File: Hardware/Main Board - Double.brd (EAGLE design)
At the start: 124.5 x 73.7 mm, 112 parts, among them J1 MICROMOD-2222-C, J10 MICRO-SD-PUSH-PUSH-EXT-PIN, J2 Vertical Qwiic Connector, J4 QWIIC_RIGHT_ANGLE, J5 CORTEX_JTAG_DEBUG_MINIMUM_PTH, J6 MICROMOD_FUNCTION_MAIN, J7 MICROMOD_FUNCTION_MAIN, Q1 3.1A/30V/105mΩ, U1 STG3856QTR, U2 MCP73831, U5 AP7361C-33

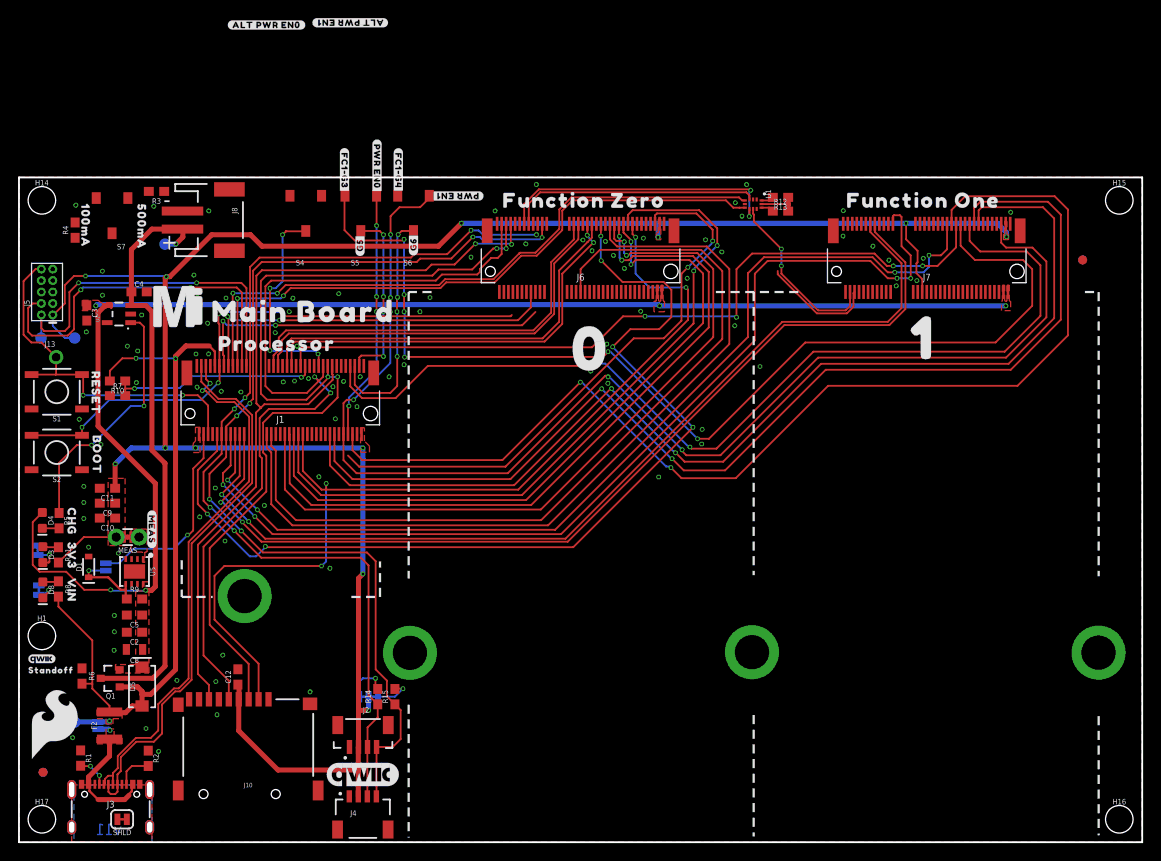
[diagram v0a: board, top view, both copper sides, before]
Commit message: Routes airwires
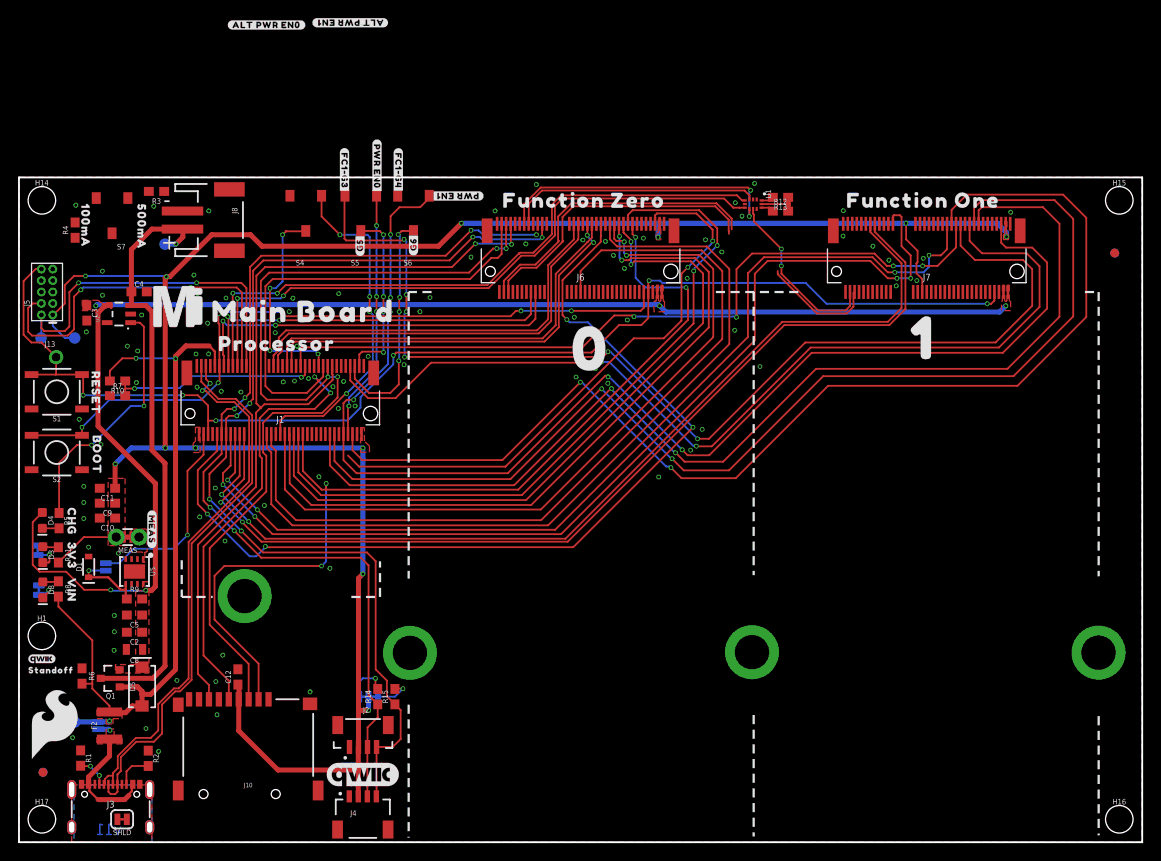
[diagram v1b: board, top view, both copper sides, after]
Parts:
- moved FD1 3.64 mm to (121.4, 65.3)
- moved FD2 3.64 mm to (121.4, 65.3)
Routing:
- net !RESET!: track 40.9 -> 140.2 mm, vias 2 -> 6
- net A1-PROCESSOR/!CS0!-ALT: track 0.00 -> 37.3 mm, vias 0 -> 4
- net RX1-AUX_TX-FC0-PLEX: track 0.00 -> 33.8 mm
- net TX1-AUX_RX-FC0-PLEX: track 0.00 -> 33.0 mm
- net !BOOT!: track 64.2 -> 80.9 mm, vias 4 -> 6
- net D0-PROCESSOR: track 108.7 -> 103.5 mm, vias 6 -> 4
- net RTS1-PROCESSOR: track 40.4 -> 43.1 mm
- net !CS1!-PROCESSOR: track 125.7 -> 128.2 mm
- net SPI_SDO1-PROCESSOR: track 123.0 -> 125.4 mm
- net G7-PROCESSOR: track 107.3 -> 106.0 mm
- net TX1-PROCESSOR: track 70.7 -> 71.5 mm
- net RX1-PROCESSOR: track 69.9 -> 70.7 mm
- net SPI_SCK1-PROCESSOR: track 120.6 -> 121.4 mm
- net G5-PROCESSOR: track 119.4 -> 120.2 mm
- net VCC: track 156.5 -> 157.0 mm
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
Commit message: Large rework in which many of the traces were routed to leave more space between them.
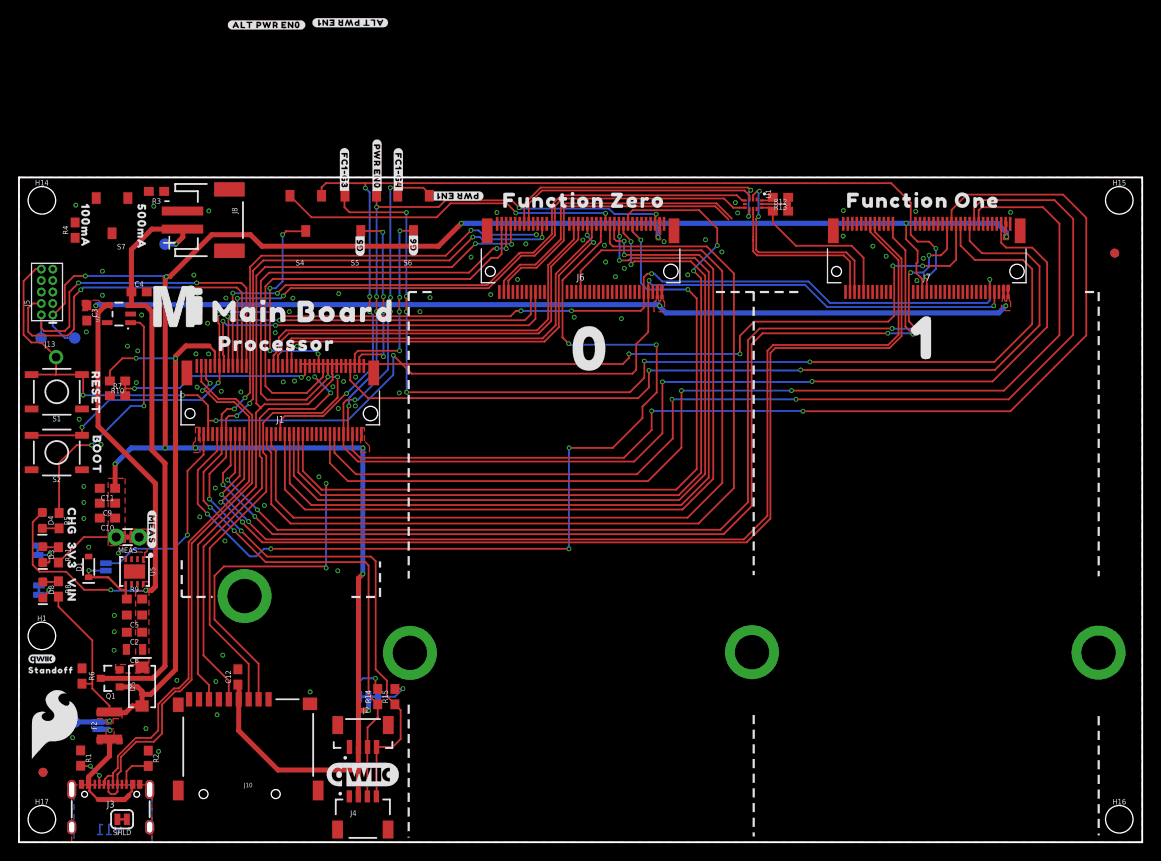
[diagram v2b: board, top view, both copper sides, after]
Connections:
- removed net PWR_EN0: J6.71
- net SDIO_DATA2/PWR_EN0_ALT: now also J6.71
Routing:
- net A1-PROCESSOR/!CS0!-ALT: track 37.3 -> 114.6 mm, vias 4 -> 6
- net PWR_EN0: track 63.8 -> 0.00 mm, vias 2 -> 0
- net !BOOT!: track 80.9 -> 126.2 mm, vias 6 -> 8
- net !CS0!-PROCESSOR: track 0.00 -> 38.3 mm, vias 0 -> 2
- net SDIO_DATA2/PWR_EN0_ALT: track 27.7 -> 60.8 mm, vias 4 -> 6
- net !DFU-FC1!: track 1.41 -> 18.1 mm
- net RX2-PROCESSOR: track 106.3 -> 118.3 mm
- net TX2-PROCESSOR: track 107.9 -> 119.8 mm
- net G4-PROCESSOR/SD_CARD_!CS!: track 109.3 -> 120.9 mm
- net G3-PROCESSOR: track 80.5 -> 91.4 mm
- net TX1-AUX_RX-FC1-PLEX: track 12.5 -> 22.9 mm, vias 0 -> 2
- net PWM0-PROCESSOR: track 92.7 -> 102.8 mm
- net G2-PROCESSOR: track 78.2 -> 88.4 mm
- net G1-PROCESSOR: track 81.8 -> 91.8 mm
- net D1-PROCESSOR: track 109.4 -> 119.1 mm, vias 4 -> 6
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
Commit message: Routes more airwires
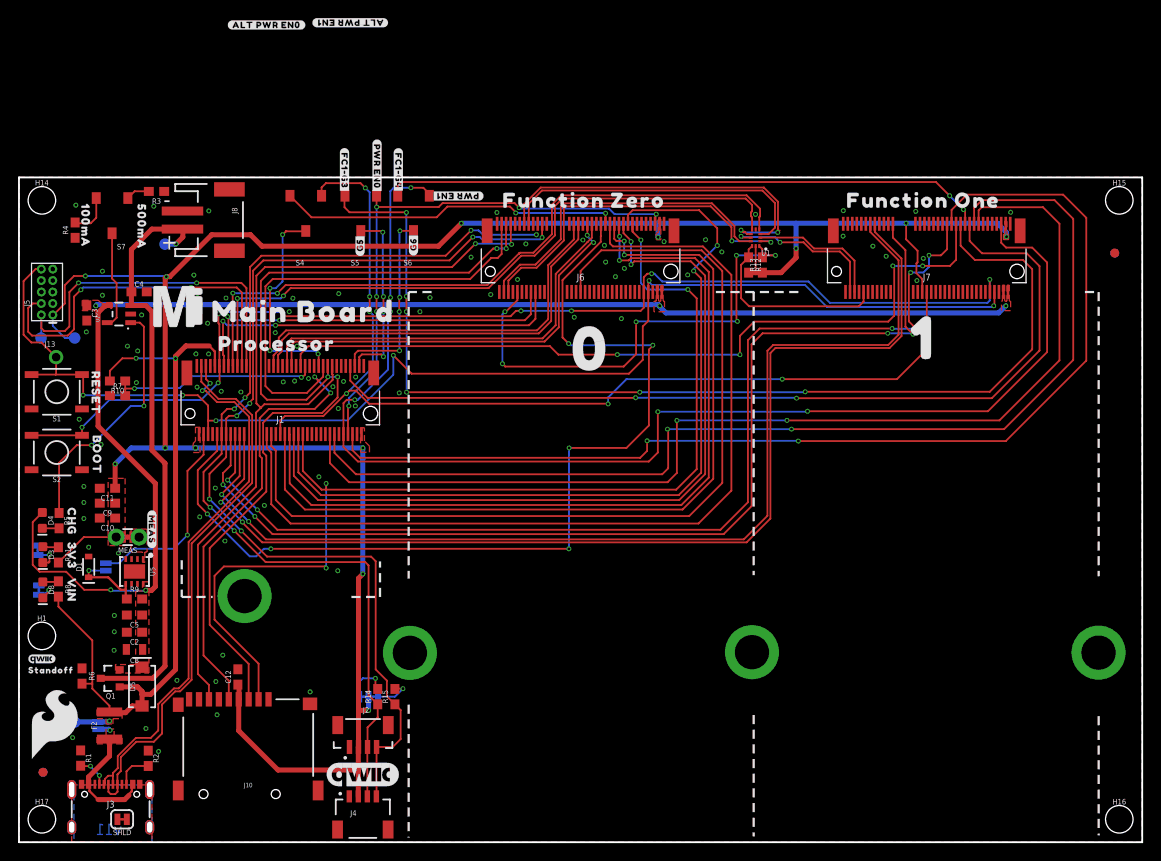
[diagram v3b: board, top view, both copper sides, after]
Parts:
- moved R13 7.76 mm to (82.4, 64.0), turned to 90 degrees
- moved R12 6.93 mm to (80.8, 64.0), turned to 270 degrees
- moved U1 3.69 mm to (81.6, 67.0), turned to 180 degrees
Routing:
- net G6-PROCESSOR: track 0.00 -> 66.9 mm, vias 0 -> 2
- net !DFU-FC0!: track 1.39 -> 53.7 mm, vias 0 -> 6
- net N$6: track 0.00 -> 10.8 mm
- net RX1-PROCESSOR-PLEX: track 32.0 -> 40.9 mm
- net 3.3V: track 250.9 -> 259.2 mm, vias 12 -> 13
- net TX1-AUX_RX-FC1-PLEX: track 22.9 -> 15.0 mm, vias 2 -> 0
- net TX1-AUX_RX-FC0-PLEX: track 31.8 -> 39.6 mm, vias 0 -> 2
- net TX1-PROCESSOR-PLEX: track 28.0 -> 35.3 mm
- net N$9: track 0.00 -> 4.81 mm
- net TX1-PROCESSOR: track 71.5 -> 75.9 mm
- net RX1-AUX_TX-FC0-PLEX: track 32.9 -> 36.7 mm
- net RX1-PROCESSOR: track 70.7 -> 74.2 mm
- net !DFU-FC1!: track 18.1 -> 21.5 mm
- net N$8: track 0.02 -> 2.64 mm
- net SPI_SDO1-PROCESSOR: track 120.8 -> 122.4 mm
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
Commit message: Routes more airwires
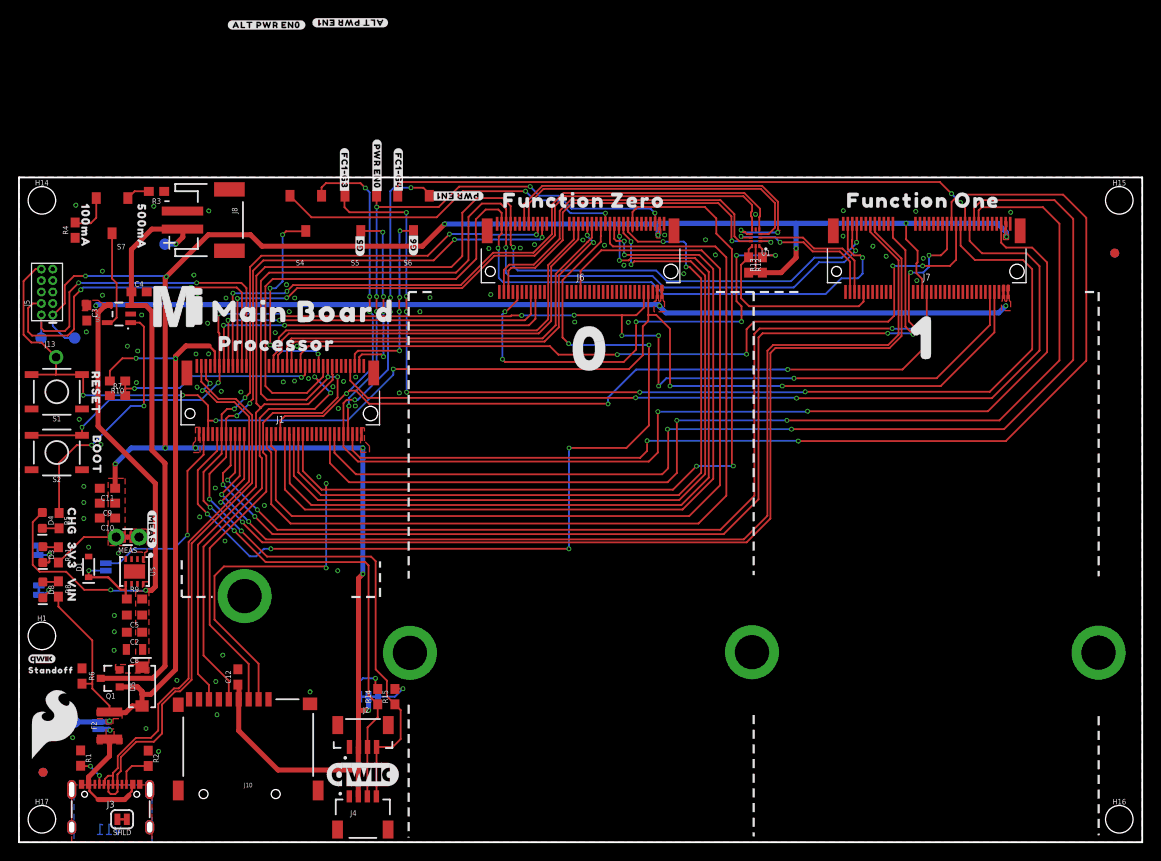
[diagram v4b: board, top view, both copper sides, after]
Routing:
- net SPI_PROCESSOR_SCK: track 98.0 -> 155.5 mm, vias 2 -> 4
- net SPI_PROCESSOR_SDO: track 101.7 -> 155.7 mm
- net SPI_PROCESSOR_SDI: track 93.5 -> 145.6 mm
- net G4-PROCESSOR/SD_CARD_!CS!: track 120.9 -> 132.9 mm
- net !BOOT!: track 126.2 -> 135.9 mm, vias 8 -> 10
- net !RESET!: track 145.0 -> 152.0 mm
- net G3-PROCESSOR: track 91.4 -> 85.1 mm
- net SDIO_DATA2/PWR_EN0_ALT: track 60.5 -> 61.9 mm
- net RX1-AUX_TX-FC0-PLEX: track 36.7 -> 38.1 mm
- net !CS0!-PROCESSOR: track 38.0 -> 39.3 mm
- net TX1-AUX_RX-FC0-PLEX: track 39.6 -> 40.9 mm
- net I2C_SDA: track 110.4 -> 111.1 mm
- net RTS1-PROCESSOR: track 43.1 -> 42.4 mm
- net CTS1-PROCESSOR: track 42.0 -> 41.4 mm
- net D0-PROCESSOR: track 107.4 -> 106.8 mm
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
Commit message: Routes more air wires, cleans up DRC
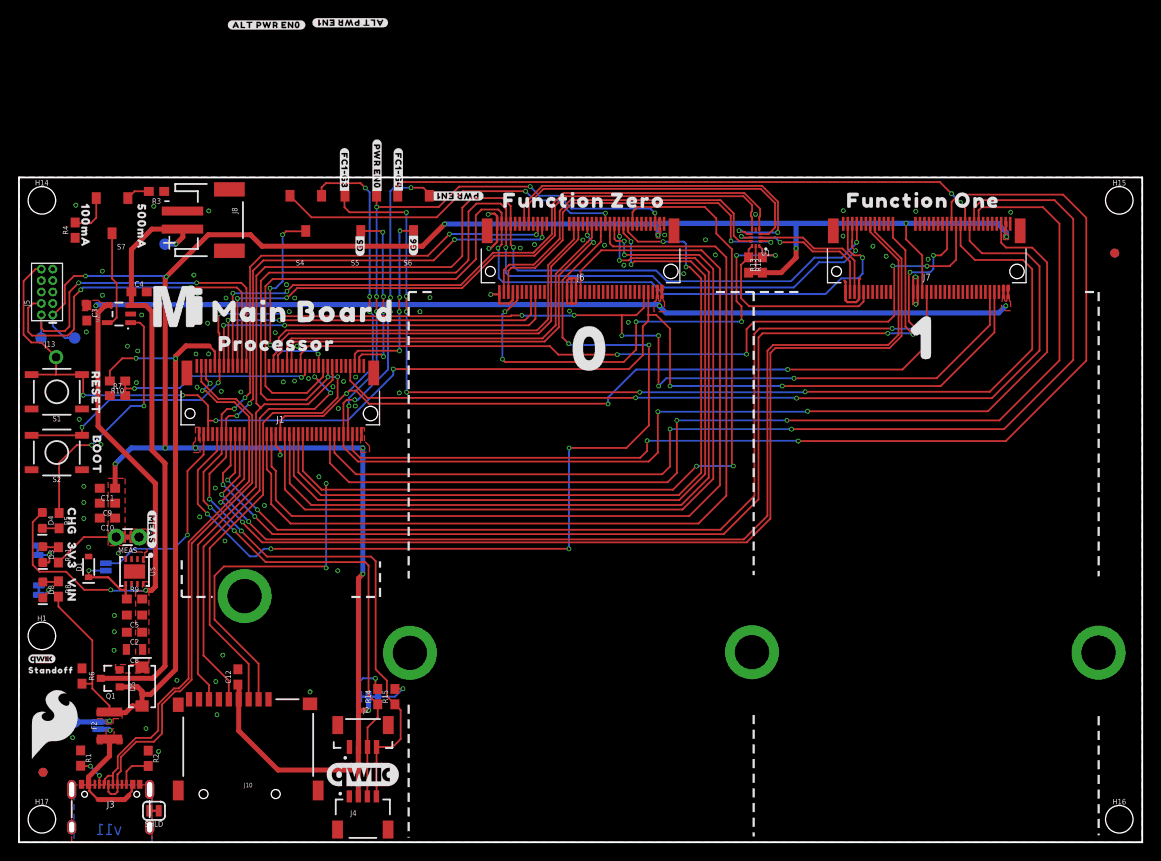
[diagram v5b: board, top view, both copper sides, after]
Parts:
- moved SHLD 3.65 mm to (15.0, 3.48)
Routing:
- net GND: track 0.00 -> 36.1 mm, vias 81 -> 84
- net G4-PROCESSOR/SD_CARD_!CS!: track 132.9 -> 132.0 mm

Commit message: Routes the last of the iar wires
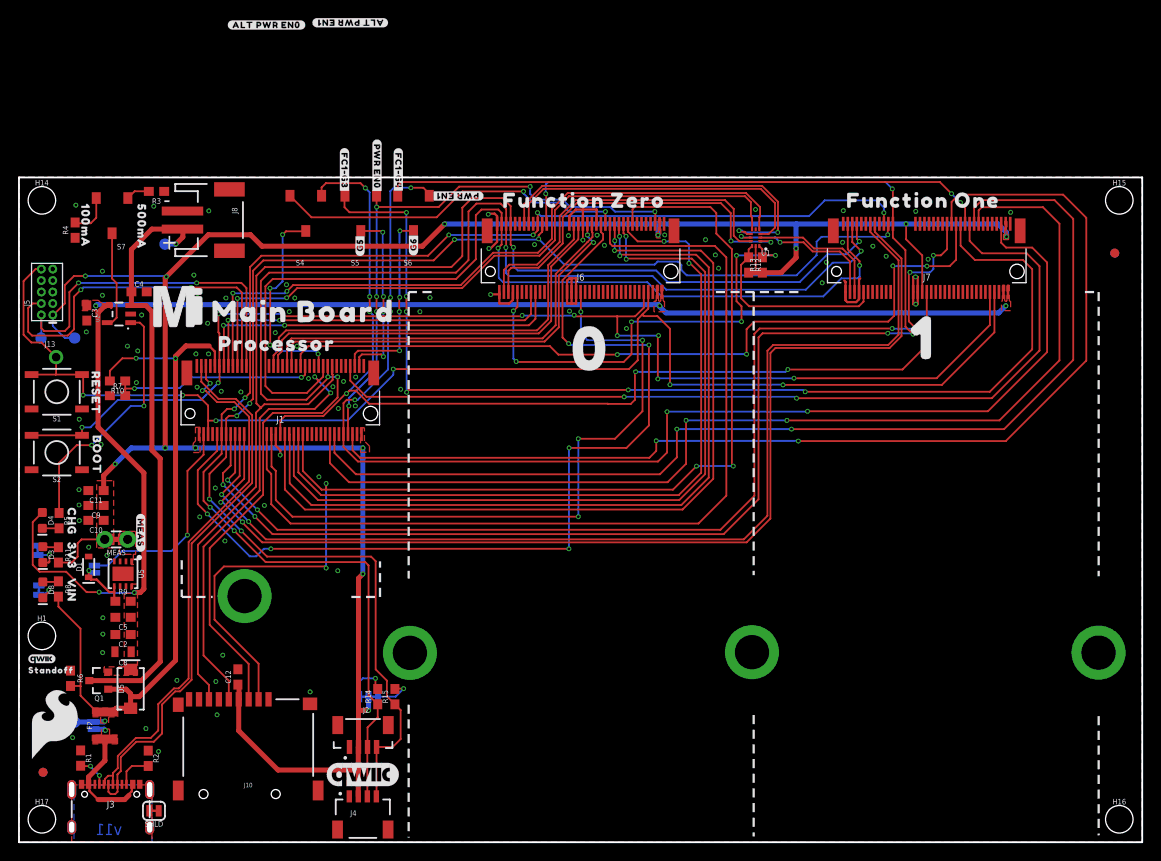
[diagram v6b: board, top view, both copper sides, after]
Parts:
- moved U$33 1.30 mm to (13.5, 34.3)
- moved C2 1.30 mm to (11.5, 23.0)
- moved C8 1.30 mm to (11.5, 21.1)
- moved R9 1.30 mm to (11.5, 26.7)
- moved U$1 1.30 mm to (11.7, 30.2)
- moved C5 1.30 mm to (11.5, 24.9)
- moved U5 1.30 mm to (11.5, 29.7)
- moved R6 1.30 mm to (5.71, 18.2)
- moved D5 1.30 mm to (12.4, 17.0)
- moved Q1 1.30 mm to (8.89, 17.9)
- moved VE 1.30 mm to (8.36, 30.3)
- moved C10 1.30 mm to (8.53, 35.7)
- moved C11 1.30 mm to (8.53, 39.0)
- moved C9 1.30 mm to (8.53, 37.3)
- moved MEAS 1.30 mm to (10.8, 33.6)
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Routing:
- net I2C_!INT!: track 117.7 -> 164.8 mm, vias 4 -> 6
- net I2C_SCL: track 113.6 -> 158.4 mm, vias 6 -> 7
- net I2C_SDA: track 111.1 -> 153.5 mm, vias 6 -> 8
- net A0-PROCESSOR: track 102.4 -> 78.4 mm, vias 0 -> 4
- net GND: track 36.1 -> 45.3 mm
- net 3.3V_EN_VE: track 9.04 -> 6.71 mm
- net !DFU-FC0!: track 53.4 -> 51.7 mm
- net VCC: track 157.2 -> 155.8 mm
- net 3.3V_EN: track 22.3 -> 23.6 mm
- net A1-PROCESSOR/!CS0!-ALT: track 114.7 -> 116.0 mm
- net SPI_PROCESSOR_SDO: track 155.7 -> 156.8 mm
- net SPI_SDO1-PROCESSOR: track 122.2 -> 121.6 mm
- net SPI_SCK1-PROCESSOR: track 120.4 -> 119.8 mm
- net SDIO_DATA2/PWR_EN0_ALT: track 61.9 -> 62.5 mm
- net !BOOT!: track 135.9 -> 135.4 mm
